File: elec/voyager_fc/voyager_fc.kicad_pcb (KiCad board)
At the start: 6 copper layers, 65 x 56 mm, 173 parts, among them J1 Raspberry Pi 5 Connector, J10 BM04B-GHS-TBT_LF__SN__N_, J11 BM04B-GHS-TBT_LF__SN__N_, J12 BM04B-GHS-TBT_LF__SN__N_, J13 BM04B-GHS-TBT_LF__SN__N_, J14 BM03B-GHS-TBT_LF__SN__N_, J15 BM03B-GHS-TBT_LF__SN__N_, J16 BM03B-GHS-TBT_LF__SN__N_, J17 BM03B-GHS-TBT_LF__SN__N_, J18 BM02B-GHS-TBT_LF__SN__N_, J19 BM02B-GHS-TBT_LF__SN__N_, J2 Pi Power Connect, J20 BM02B-GHS-TBT_LF__SN__N_, J21 BM06B-GHS-TBT_LF__SN__N_, J22 BM06B-GHS-TBT_LF__SN__N_, J23 BM06B-GHS-TBT_LF__SN__N_, J24 AUX Leak, J3 AUX Power Connect, J4 PWM Power Rail 1, J5 PWM GND Rail 1, J6 PWM Signal Rail 1, J7 PWM Power Rail 2, J8 PWM GND Rail 2, J9 PWM Signal Rail 2, Q3 BSS138, Q4 BSS138, Q5 MMBT3906, U1 TCA9548APWR, U10 LTC4311CDC_TRMPBF, U11 LTC4311CDC_TRMPBF, U12 LTC4311CDC_TRMPBF, U13 LTC4311CDC_TRMPBF, U14 TXS0102YZP, U15 TXS0102YZP, U16 TXS0102YZP, U17 TXS0102YZP, U2 PCA9685PW, U3 PCA9685PW, U4 BME680, U5 ICM-20948, U6 TPS2121RUXR, U7 AMS1117-3.3, U8 ADS1015IDGS, U9 AMS1117-1.8, X1 SG-8002CE

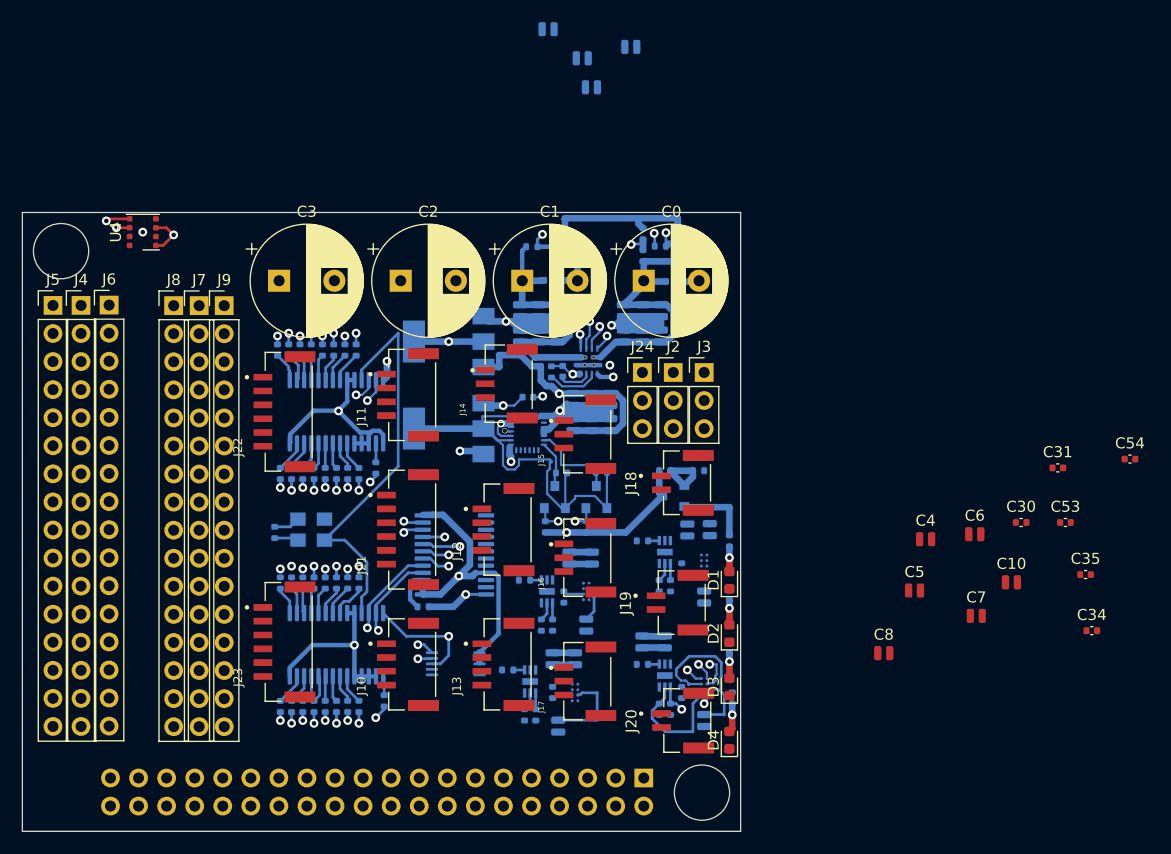
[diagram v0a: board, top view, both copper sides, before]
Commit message: Place all components and start route
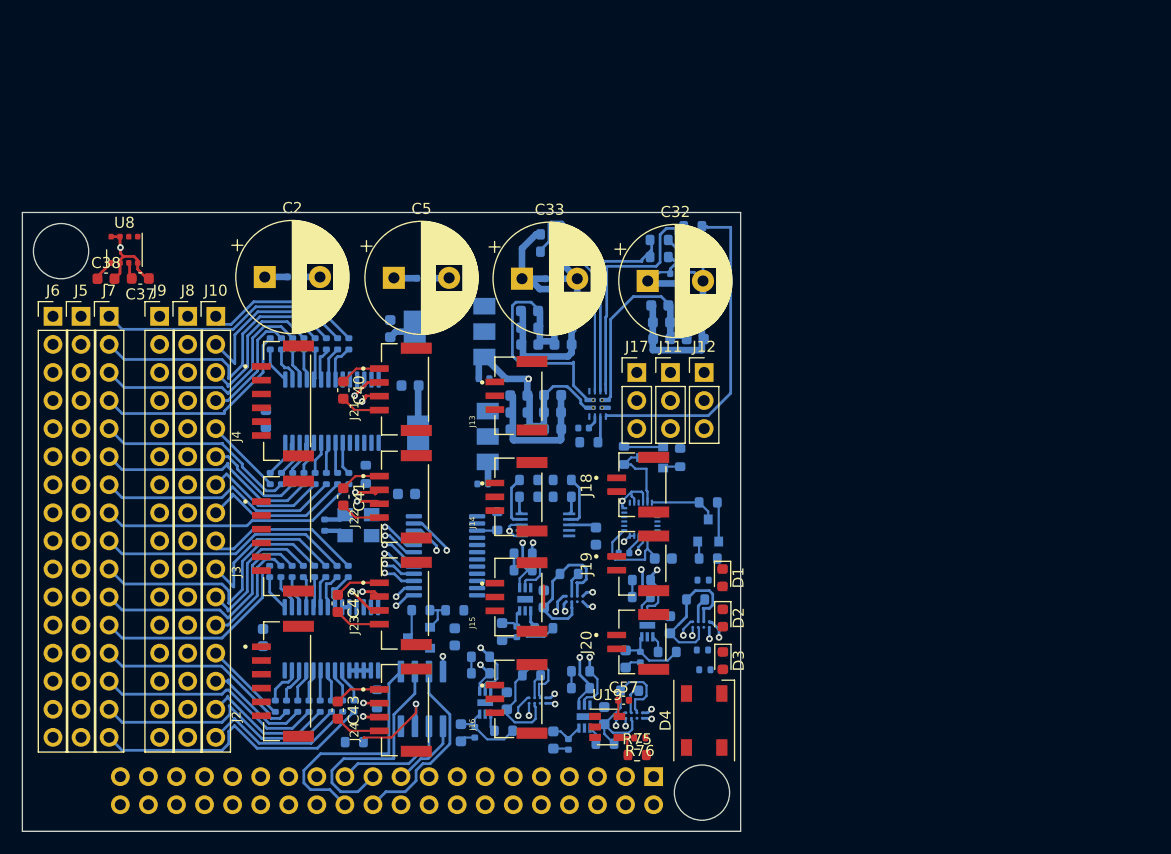
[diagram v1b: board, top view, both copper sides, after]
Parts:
- removed C0: 4700uF, Capacitor_THT:CP_Radial_D10.0mm_P5.00mm
- removed Q4: BSS138, Package_TO_SOT_SMD:SOT-23
- removed Q5: MMBT3906, Package_TO_SOT_SMD:SOT-23
- removed R0: 10k, Resistor_SMD:R_0402_1005Metric
- added C47: 10uF, Capacitor_SMD:C_0603_1608Metric, B.Cu at (161.2, 110.8)
- added C55: 10uF, Capacitor_SMD:C_0603_1608Metric, B.Cu at (176.4, 110.1)
- added C56: 10uF, Capacitor_SMD:C_0603_1608Metric, B.Cu at (170.4, 118.4)
- added C57: 100nF, Capacitor_SMD:C_0402_1005Metric, F.Cu at (172.2, 117.0)
- added Q1: MMBT3906, Package_TO_SOT_SMD:SOT-23, B.Cu at (153.7, 111.3)
- added Q2: BSS138, Package_TO_SOT_SMD:SOT-23, B.Cu at (174.8, 95.0)
- added R1: 220, Resistor_SMD:R_0402_1005Metric, B.Cu at (179.4, 106.1)
- added R4: 220, Resistor_SMD:R_0402_1005Metric, B.Cu at (147.8, 117.5)
- added R5: 220, Resistor_SMD:R_0402_1005Metric, B.Cu at (146.7, 117.5)
- added R6: 220, Resistor_SMD:R_0402_1005Metric, B.Cu at (145.7, 117.5)
- added R7: 220, Resistor_SMD:R_0402_1005Metric, B.Cu at (144.7, 117.5)
- added R75: 470, Resistor_SMD:R_0603_1608Metric, F.Cu at (173.4, 121.9)
- added R76: 470, Resistor_SMD:R_0402_1005Metric, F.Cu at (173.6, 120.4)
- added U18: TXS0102YZP, Package_BGA:Texas_DSBGA-8_0.9x1.9mm_Layout2x4_P0.5mm, B.Cu at (179.2, 110.1)
- added U19: SN74LV1T34DBV, Package_TO_SOT_SMD:SOT-23-5, F.Cu at (170.7, 119.4)
- C1: value 4700uF -> 0.1uF; footprint Capacitor_THT:CP_Radial_D10.0mm_P5.00mm -> Capacitor_SMD:C_0402_1005Metric; moved to B.Cu
- C10, C6, C7, C8: footprint Capacitor_SMD:C_0504_1310Metric -> Capacitor_SMD:C_0603_1608Metric; moved to B.Cu
- C11: value 1nF -> 10uF; footprint Capacitor_SMD:C_0402_1005Metric -> Capacitor_SMD:C_0603_1608Metric
- C12, C13, C14, C15, C16, C17, C18, C21, C23, C24, C25, C26, C27, C28, C29, C44, C45, C46, C48: footprint Capacitor_SMD:C_0504_1310Metric -> Capacitor_SMD:C_0603_1608Metric
- C19, C22: value 10uF -> 1uF; footprint Capacitor_SMD:C_0504_1310Metric -> Capacitor_SMD:C_0402_1005Metric
- C20: value 10uF -> 1nF; footprint Capacitor_SMD:C_0504_1310Metric -> Capacitor_SMD:C_0402_1005Metric
- C3: value 4700uF -> 10uF; footprint Capacitor_THT:CP_Radial_D10.0mm_P5.00mm -> Capacitor_SMD:C_0603_1608Metric; moved to B.Cu
- C30: value 10uF -> 0.1uF; moved to B.Cu
- C31: value 1uF -> 0.1uF; moved to B.Cu
- C32, C33: value 0.1uF -> 4700uF; footprint Capacitor_SMD:C_0402_1005Metric -> Capacitor_THT:CP_Radial_D10.0mm_P5.00mm; moved to F.Cu
- C34, C35: value 0.1uF -> 10uF; footprint Capacitor_SMD:C_0402_1005Metric -> Capacitor_SMD:C_0603_1608Metric; moved to B.Cu
- C36: value 10uF -> 0.1uf; footprint Capacitor_SMD:C_0504_1310Metric -> Capacitor_SMD:C_0402_1005Metric
- C37, C41, C43: value 0.1uF -> 10uF; footprint Capacitor_SMD:C_0504_1310Metric -> Capacitor_SMD:C_0603_1608Metric; moved to F.Cu
- C38, C40, C42: footprint Capacitor_SMD:C_0504_1310Metric -> Capacitor_SMD:C_0603_1608Metric; moved to F.Cu
- C39: value 0.1uF -> 10uF; footprint Capacitor_SMD:C_0504_1310Metric -> Capacitor_SMD:C_0603_1608Metric
- C4: value 10uF -> 0.1uF; footprint Capacitor_SMD:C_0504_1310Metric -> Capacitor_SMD:C_0402_1005Metric; moved to B.Cu
- C49, C50, C51, C52: value 10uF -> 0.1uF; footprint Capacitor_SMD:C_0504_1310Metric -> Capacitor_SMD:C_0402_1005Metric
- C5: value 10uF -> 4700uF; footprint Capacitor_SMD:C_0504_1310Metric -> Capacitor_THT:CP_Radial_D10.0mm_P5.00mm
- C53: value 1uF -> 10uF; footprint Capacitor_SMD:C_0402_1005Metric -> Capacitor_SMD:C_0603_1608Metric; moved to B.Cu
- C54: footprint Capacitor_SMD:C_0402_1005Metric -> Capacitor_SMD:C_0603_1608Metric; moved to B.Cu
- C9: value 0.1uf -> 10uF; footprint Capacitor_SMD:C_0402_1005Metric -> Capacitor_SMD:C_0603_1608Metric
- D1: value WHITE -> RED
- D2: value RED -> YELLOW
- D3: value YELLOW -> WHITE
- D4: value GREEN -> SK6812; footprint LED_SMD:LED_0603_1608Metric -> LED_SMD:LED_SK6812_PLCC4_5.0x5.0mm_P3.2mm
- J10: value BM04B-GHS-TBT_LF__SN__N_ -> PWM Signal Rail 1; footprint BM04B-GHS-TBT_LF__SN__N_:JST_BM04B-GHS-TBT_LF__SN__N_ -> Connector_PinHeader_2.54mm:PinHeader_1x16_P2.54mm_Vertical
- J11: value BM04B-GHS-TBT_LF__SN__N_ -> Pi Power Connect; footprint BM04B-GHS-TBT_LF__SN__N_:JST_BM04B-GHS-TBT_LF__SN__N_ -> Connector_PinHeader_2.54mm:PinHeader_1x03_P2.54mm_Vertical
- J12: value BM04B-GHS-TBT_LF__SN__N_ -> AUX Power Connect; footprint BM04B-GHS-TBT_LF__SN__N_:JST_BM04B-GHS-TBT_LF__SN__N_ -> Connector_PinHeader_2.54mm:PinHeader_1x03_P2.54mm_Vertical
- J13: value BM04B-GHS-TBT_LF__SN__N_ -> BM03B-GHS-TBT_LF__SN__N_; footprint BM04B-GHS-TBT_LF__SN__N_:JST_BM04B-GHS-TBT_LF__SN__N_ -> BM03B-GHS-TBT_LF__SN__N_:CONN_BM03B-GHS-TBT_LF__SN__N_
- J17: value BM03B-GHS-TBT_LF__SN__N_ -> AUX Leak; footprint BM03B-GHS-TBT_LF__SN__N_:CONN_BM03B-GHS-TBT_LF__SN__N_ -> Connector_PinHeader_2.54mm:PinHeader_1x03_P2.54mm_Vertical
- J2: value Pi Power Connect -> BM06B-GHS-TBT_LF__SN__N_; footprint Connector_PinHeader_2.54mm:PinHeader_1x03_P2.54mm_Vertical -> BM06B-GHS-TBT_LF__SN__N_:JST_BM06B-GHS-TBT_LF__SN__N_
- J21, J22, J23: value BM06B-GHS-TBT_LF__SN__N_ -> BM04B-GHS-TBT_LF__SN__N_; footprint BM06B-GHS-TBT_LF__SN__N_:JST_BM06B-GHS-TBT_LF__SN__N_ -> BM04B-GHS-TBT_LF__SN__N_:JST_BM04B-GHS-TBT_LF__SN__N_
- J24: value AUX Leak -> BM04B-GHS-TBT_LF__SN__N_; footprint Connector_PinHeader_2.54mm:PinHeader_1x03_P2.54mm_Vertical -> BM04B-GHS-TBT_LF__SN__N_:JST_BM04B-GHS-TBT_LF__SN__N_
- J3: value AUX Power Connect -> BM06B-GHS-TBT_LF__SN__N_; footprint Connector_PinHeader_2.54mm:PinHeader_1x03_P2.54mm_Vertical -> BM06B-GHS-TBT_LF__SN__N_:JST_BM06B-GHS-TBT_LF__SN__N_
- J4: value PWM Power Rail 1 -> BM06B-GHS-TBT_LF__SN__N_; footprint Connector_PinHeader_2.54mm:PinHeader_1x16_P2.54mm_Vertical -> BM06B-GHS-TBT_LF__SN__N_:JST_BM06B-GHS-TBT_LF__SN__N_
- J5: value PWM GND Rail 1 -> PWM Power Rail 2
- J6: value PWM Signal Rail 1 -> PWM GND Rail 2
- J7: value PWM Power Rail 2 -> PWM Signal Rail 2
- J8: value PWM GND Rail 2 -> PWM Power Rail 1
- J9: value PWM Signal Rail 2 -> PWM GND Rail 1
- R10, R11, R2, R8, R9: value 10k -> 220
- R20: value 220 -> 200
- R21, R55, R56, R57: value 220 -> 10k; footprint Resistor_SMD:R_0402_1005Metric -> Resistor_SMD:R_0603_1608Metric
- R3, R59, R60, R61, R62, R63, R64, R65, R66, R67, R68, R69, R70, R71, R72, R73, R74: footprint Resistor_SMD:R_0402_1005Metric -> Resistor_SMD:R_0603_1608Metric
- R38: value 220 -> 4.99k; footprint Resistor_SMD:R_0402_1005Metric -> Resistor_SMD:R_0603_1608Metric
- R39, R41: value 220 -> 1.15k; footprint Resistor_SMD:R_0402_1005Metric -> Resistor_SMD:R_0603_1608Metric
- R40: value 220 -> 4.99K; footprint Resistor_SMD:R_0402_1005Metric -> Resistor_SMD:R_0603_1608Metric
- R42: value 220 -> 4.32k; footprint Resistor_SMD:R_0402_1005Metric -> Resistor_SMD:R_0603_1608Metric
- R43: value 220 -> 10.2k; footprint Resistor_SMD:R_0402_1005Metric -> Resistor_SMD:R_0603_1608Metric
- R44: value 1K -> 36.5k; footprint Resistor_SMD:R_0402_1005Metric -> Resistor_SMD:R_0603_1608Metric
- R45: value 20K -> 19.6k; footprint Resistor_SMD:R_0402_1005Metric -> Resistor_SMD:R_0603_1608Metric
- R46: value 220 -> 470k; footprint Resistor_SMD:R_0402_1005Metric -> Resistor_SMD:R_0603_1608Metric
- R47: value 4.99K -> 470k; footprint Resistor_SMD:R_0402_1005Metric -> Resistor_SMD:R_0603_1608Metric
- R48: value 4.32k -> 470k; footprint Resistor_SMD:R_0402_1005Metric -> Resistor_SMD:R_0603_1608Metric
- R49: value 36.5k -> 470k; footprint Resistor_SMD:R_0402_1005Metric -> Resistor_SMD:R_0603_1608Metric
- R50: value 1.15k -> 20K; footprint Resistor_SMD:R_0402_1005Metric -> Resistor_SMD:R_0603_1608Metric
- R51: value 10.2k -> 1K; footprint Resistor_SMD:R_0402_1005Metric -> Resistor_SMD:R_0603_1608Metric
- R52: value 4.99k -> 220
- R53: value 1.15k -> 10k; footprint Resistor_SMD:R_0402_1005Metric -> Resistor_SMD:R_0603_1608Metric
- R54: value 19.6k -> 10k; footprint Resistor_SMD:R_0402_1005Metric -> Resistor_SMD:R_0603_1608Metric
- R58: value 200 -> 10k; footprint Resistor_SMD:R_0402_1005Metric -> Resistor_SMD:R_0603_1608Metric
- U1: value TCA9548APWR -> PCA9685PW; footprint Package_SO:TSSOP-24_4.4x7.8mm_P0.65mm -> Package_SO:TSSOP-28_4.4x9.7mm_P0.65mm
- U10: value LTC4311CDC_TRMPBF -> TCA9548APWR; footprint footprint:DFN-6_DC -> Package_SO:TSSOP-24_4.4x7.8mm_P0.65mm
- U14: value TXS0102YZP -> LTC4311CDC_TRMPBF; footprint Package_BGA:Texas_DSBGA-8_0.9x1.9mm_Layout2x4_P0.5mm -> footprint:DFN-6_DC
- U3: value PCA9685PW -> AMS1117-1.8; footprint Package_SO:TSSOP-28_4.4x9.7mm_P0.65mm -> Package_TO_SOT_SMD:SOT-223-3_TabPin2
- U4: value BME680 -> TPS2121RUXR; footprint Package_LGA:Bosch_LGA-8_3x3mm_P0.8mm_ClockwisePinNumbering -> TPS2121RUXR:IC_TPS2121RUXR; moved to B.Cu
- U5: value ICM-20948 -> AMS1117-3.3; footprint Sensor_Motion:InvenSense_QFN-24_3x3mm_P0.4mm -> Package_TO_SOT_SMD:SOT-223-3_TabPin2
- U6: value TPS2121RUXR -> ADS1015IDGS; footprint TPS2121RUXR:IC_TPS2121RUXR -> Package_SO:TSSOP-10_3x3mm_P0.5mm
- U7: value AMS1117-3.3 -> ICM-20948; footprint Package_TO_SOT_SMD:SOT-223-3_TabPin2 -> Sensor_Motion:InvenSense_QFN-24_3x3mm_P0.4mm
- U8: value ADS1015IDGS -> BME680; footprint Package_SO:TSSOP-10_3x3mm_P0.5mm -> Package_LGA:Bosch_LGA-8_3x3mm_P0.8mm_ClockwisePinNumbering; moved to F.Cu
- U9: value AMS1117-1.8 -> MB85RS512T; footprint Package_TO_SOT_SMD:SOT-223-3_TabPin2 -> MB85RS512TPNF-G-JNERE1:SOIC127P600X88-8N
- moved C6 65.1 mm to (139.5, 111.3), turned to 90 degrees
- moved C46 64.2 mm to (157.5, 119.9), turned to 270 degrees
- moved C45 63.1 mm to (165.8, 120.6), turned to 270 degrees
- moved C4 62.0 mm to (142.3, 78.7)
- moved C38 60.3 mm to (125.3, 78.8), turned to 0 degrees
- moved C5 55.0 mm to (151.4, 78.7)
- moved C54 54.5 mm to (165.0, 107.8), turned to 90 degrees
- moved C48 54.5 mm to (172.4, 113.2), turned to 270 degrees
- moved C53 53.1 mm to (161.6, 117.0), turned to 90 degrees
- moved C37 52.3 mm to (128.4, 78.8), turned to 180 degrees
- moved C31 49.0 mm to (165.6, 78.8)
- moved U8 48.0 mm to (127.0, 76.2), turned to 0 degrees
- moved C10 46.7 mm to (166.7, 83.2)
- moved C34 45.7 mm to (169.7, 102.1), turned to 90 degrees
- moved U4 44.0 mm to (169.8, 90.1), turned to 0 degrees
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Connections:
- net PI_CE1 renamed Net-(J1-Pad26)
- net PI_CLK renamed Net-(J1-Pad12)
- net PI_DIN renamed Net-(J1-Pad38)
- net PI_DOUT renamed Net-(J1-Pad40)
- net PI_FS renamed Net-(J1-Pad35)
- net PI_GPIO22 renamed Net-(J1-Pad15)
- net PI_GPIO23 renamed Net-(J1-Pad16)
- net PI_GPIO24 renamed Net-(J1-Pad18)
- net PI_GPIO27 renamed Net-(J1-Pad13)
- net PI_GPIO4 renamed Net-(J1-Pad7)
- net PI_IDSC renamed Net-(J1-Pad28)
- net PI_IDSD renamed Net-(J1-Pad27)
- C1 pad 1: 5VAux -> +5V
- C10 pad 1: GND -> /PREG/5VAux
- C10 pad 2: +5V -> GND
- C11 pad 1: Net-(C11-Pad1) -> /PREG/5VMain
- C12 pad 1: 5VAux -> /PREG/5VAux
- C13 pad 1: 5VAux -> /PREG/5VMain
- C14 pad 1: 5VAux -> /PREG/5VAux
- C15 pad 1: 5VAux -> /PREG/5VMain
- C16 pad 1: 5VAux -> /PREG/5VAux
- C17 pad 1: 5VAux -> /PREG/5VMain
- C18 pad 1: 5VMain -> /PREG/5VAux
- C19 pad 1: 5VMain -> +3V3
- C20 pad 1: 5VMain -> Net-(C20-Pad1)
- C21 pad 1: 5VMain -> GND
- C21 pad 2: GND -> +1V8
- C22 pad 1: 5VMain -> +5V
- C23 pad 1: 5VMain -> +5V
- C25 pad 1: +5V -> GND
- C25 pad 2: GND -> +3V3
- C3 pad 1: +5V -> GND
- C3 pad 2: GND -> +5V
- C30 pad 1: GND -> /PREG/5VMain
- C30 pad 2: +3V3 -> GND
- C31 pad 1: +5V -> /PREG/5VAux
- C32 pad 1: 5VMain -> /PREG/5VMain
- C33 pad 1: 5VAux -> /PREG/5VAux
- C34 pad 1: +5V -> GND
- C34 pad 2: GND -> +5V
- C35 pad 1: +5V -> GND
- C35 pad 2: GND -> +1V8
- C36 pad 1: +3V3 -> GND
- C36 pad 2: GND -> Net-(C36-Pad2)
- C37 pad 1: +3V3 -> GND
- C37 pad 2: GND -> +3V3
- C4 pad 1: +3V3 -> +5V
- C40 pad 1: +3V3 -> +5V
- C41 pad 1: +3V3 -> +5V
- C42 pad 1: +3V3 -> +5V
- C43 pad 1: +3V3 -> +5V
- C44 pad 1: +5V -> +3V3
- C45 pad 1: +5V -> +3V3
- C46 pad 1: +5V -> +3V3
- C48 pad 1: +5V -> +3V3
- C49 pad 1: Net-(C49-Pad1) -> +3V3
- C49 pad 2: +3V3 -> GND
- C5 pad 1: GND -> +5V
- C5 pad 2: +5V -> GND
- C50 pad 1: Net-(C50-Pad1) -> +3V3
- C50 pad 2: +3V3 -> GND
- C51 pad 1: Net-(C51-Pad1) -> +3V3
- C51 pad 2: +3V3 -> GND
- C52 pad 1: Net-(C52-Pad1) -> +3V3
- C52 pad 2: +3V3 -> GND
- C54 pad 1: GND -> +3V3
- C54 pad 2: +1V8 -> GND
- C7 pad 1: GND -> /PREG/5VMain
- C7 pad 2: +3V3 -> GND
- C8 pad 1: +3V3 -> /PREG/5VAux
- C9 pad 1: GND -> /PREG/5VMain
- C9 pad 2: Net-(C9-Pad2) -> GND
- J1 pad 10: PI_RXD -> /PI_RXD0
- J1 pad 11: PI_GPIO17 -> /PI_RXD1
- J1 pad 17: PION -> /SOFTON
- J1 pad 19: PI_MOSI -> /MOSI
- J1 pad 21: PI_MISO -> /MISO
- J1 pad 22: PI_GPIO25 -> /WP
- J1 pad 23: PI_SCLK -> /SCLK
- J1 pad 24: PI_CE0 -> /CE0
- J1 pad 29: PI_GPIO5 -> /NEODIN
- J1 pad 3: PI_SDA -> /PI_SDA
- J1 pad 31: PI_GPIO6 -> /NEORGBDIN
- J1 pad 32: PI_GPIO12 -> /PI_TXD2
- J1 pad 33: PI_GPIO13 -> /PI_RXD2
- J1 pad 36: PI_GPIO16 -> /PI_TXD1
- J1 pad 37: PI_GPIO26 -> /LEAKIN
- J1 pad 5: PI_SCL -> /PI_SCL
- J1 pad 8: PI_TXD -> /PI_TXD0
- J10 pad 1: +5V -> /PWM/PWM31
- J10 pad 2: OSC4 -> /PWM/PWM30
- J10 pad 3: OSD4 -> /PWM/PWM29
- J10 pad 4: GND -> /PWM/PWM28
- J11 pad 1: +5V -> /PREG/5VMain
- J11 pad 2: OSC7 -> GND
- J11 pad 3: OSD7 -> GND
- J12 pad 1: +5V -> /PREG/5VAux
- J12 pad 2: OSC6 -> GND
- J12 pad 3: OSD6 -> GND
- J13 pad 1: +5V -> GND
- J13 pad 2: OSC5 -> /ADS/AIN0
- J13 pad 3: OSD5 -> +3V3
- J14 pad 2: AIN0 -> /ADS/AIN1
- J15 pad 2: AIN1 -> /ADS/AIN2
- J16 pad 2: AIN2 -> /ADS/AIN3
- J17 pad 2: AIN3 -> +3V3
- J17 pad 3: +3V3 -> /LEAK/LEAK_
- J18 pad 2: LEAK_IN -> /LEAK/LEAK_
- J19 pad 2: LEAK_IN -> /LEAK/LEAK_
- J2 pad 1: 5VMain -> +5V
- J2 pad 2: GND -> /PI_TXD0
- J2 pad 3: GND -> /PI_RXD0
- J20 pad 2: LEAK_IN -> /LEAK/LEAK_
- J21 pad 2: PI_TXD -> /I2C/OSC4
- J21 pad 3: PI_RXD -> /I2C/OSD4
- J21 pad 4: Net-(J21-Pad4) -> GND
- J22 pad 2: PI_GPIO16 -> /I2C/OSC5
- J22 pad 3: PI_GPIO17 -> /I2C/OSD5
- J22 pad 4: Net-(J22-Pad4) -> GND
- J23 pad 2: PI_GPIO12 -> /I2C/OSC6
- J23 pad 3: PI_GPIO13 -> /I2C/OSD6
- J23 pad 4: Net-(J23-Pad4) -> GND
- J24 pad 1: GND -> +5V
- J24 pad 2: +3V3 -> /I2C/OSC7
- J24 pad 3: LEAK_IN -> /I2C/OSD7
- J3 pad 1: 5VAux -> +5V
- J3 pad 2: GND -> /PI_TXD1
- J3 pad 3: GND -> /PI_RXD1
- J4 pad 2: +5V -> /PI_TXD2
- J4 pad 3: +5V -> /PI_RXD2
- J4 pad 4: +5V -> Net-(J4-Pad4)
- J4 pad 5: +5V -> Net-(J4-Pad5)
- J4 pad 6: +5V -> GND
- J5 pad 1: GND -> +5V
- J5 pad 10: GND -> +5V
- J5 pad 11: GND -> +5V
- J5 pad 12: GND -> +5V
- J5 pad 13: GND -> +5V
- J5 pad 14: GND -> +5V
- J5 pad 15: GND -> +5V
- J5 pad 16: GND -> +5V
- J5 pad 2: GND -> +5V
- J5 pad 3: GND -> +5V
- J5 pad 4: GND -> +5V
- J5 pad 5: GND -> +5V
- J5 pad 6: GND -> +5V
- J5 pad 7: GND -> +5V
- J5 pad 8: GND -> +5V
- J5 pad 9: GND -> +5V
- J6 pad 1: PWM15 -> GND
- J6 pad 10: PWM6 -> GND
- J6 pad 11: PWM5 -> GND
- J6 pad 12: PWM4 -> GND
- J6 pad 13: PWM3 -> GND
- J6 pad 14: PWM2 -> GND
- J6 pad 15: PWM1 -> GND
- J6 pad 16: PWM0 -> GND
- J6 pad 2: PWM14 -> GND
- J6 pad 3: PWM13 -> GND
- J6 pad 4: PWM12 -> GND
- J6 pad 5: PWM11 -> GND
- J6 pad 6: PWM10 -> GND
- J6 pad 7: PWM9 -> GND
- J6 pad 8: PWM8 -> GND
- J6 pad 9: PWM7 -> GND
- J7 pad 1: +5V -> /PWM/PWM15
- J7 pad 10: +5V -> /PWM/PWM6
- J7 pad 11: +5V -> /PWM/PWM5
- J7 pad 12: +5V -> /PWM/PWM4
- J7 pad 13: +5V -> /PWM/PWM3
- J7 pad 14: +5V -> /PWM/PWM2
- J7 pad 15: +5V -> /PWM/PWM1
- J7 pad 16: +5V -> /PWM/PWM0
- J7 pad 2: +5V -> /PWM/PWM14
- J7 pad 3: +5V -> /PWM/PWM13
- J7 pad 4: +5V -> /PWM/PWM12
- J7 pad 5: +5V -> /PWM/PWM11
- J7 pad 6: +5V -> /PWM/PWM10
- J7 pad 7: +5V -> /PWM/PWM9
- J7 pad 8: +5V -> /PWM/PWM8
- J7 pad 9: +5V -> /PWM/PWM7
- J8 pad 1: GND -> +5V
- J8 pad 10: GND -> +5V
- J8 pad 11: GND -> +5V
- J8 pad 12: GND -> +5V
- J8 pad 13: GND -> +5V
- J8 pad 14: GND -> +5V
- J8 pad 15: GND -> +5V
- J8 pad 16: GND -> +5V
- J8 pad 2: GND -> +5V
- J8 pad 3: GND -> +5V
- J8 pad 4: GND -> +5V
- J8 pad 5: GND -> +5V
- J8 pad 6: GND -> +5V
- J8 pad 7: GND -> +5V
- J8 pad 8: GND -> +5V
- J8 pad 9: GND -> +5V
- J9 pad 1: PWM31 -> GND
- J9 pad 10: PWM22 -> GND
- J9 pad 11: PWM21 -> GND
- J9 pad 12: PWM20 -> GND
- J9 pad 13: PWM19 -> GND
- J9 pad 14: PWM18 -> GND
- J9 pad 15: PWM17 -> GND
- J9 pad 16: PWM16 -> GND
- J9 pad 2: PWM30 -> GND
- J9 pad 3: PWM29 -> GND
- J9 pad 4: PWM28 -> GND
- J9 pad 5: PWM27 -> GND
- J9 pad 6: PWM26 -> GND
- J9 pad 7: PWM25 -> GND
- J9 pad 8: PWM24 -> GND
- J9 pad 9: PWM23 -> GND
- Q3 pad 2: SD2 -> /SDIMU
- Q3 pad 3: SDL21v8 -> /IMU/SDL21V8
- R10 pad 1: +1V8 -> Net-(R10-Pad1)
- R10 pad 2: SCL21v8 -> /PWM/PWM3
- R11 pad 1: +1V8 -> Net-(R11-Pad1)
- R11 pad 2: SDL21v8 -> /PWM/PWM19
- R12 pad 2: PWM0 -> /PWM/PWM4
- R13 pad 2: PWM16 -> /PWM/PWM20
- R14 pad 2: PWM1 -> /PWM/PWM5
- R15 pad 2: PWM17 -> /PWM/PWM21
- R16 pad 2: PWM2 -> /PWM/PWM6
- R17 pad 2: PWM18 -> /PWM/PWM22
- R18 pad 2: PWM3 -> /PWM/PWM7
- R19 pad 2: PWM19 -> /PWM/PWM23
- R2 pad 1: +3V3 -> Net-(D2-Pad2)
- R2 pad 2: Net-(R2-Pad2) -> /SOFTON
- R20 pad 2: PWM4 -> +5V
- R21 pad 1: Net-(R21-Pad1) -> +3V3
- R21 pad 2: PWM20 -> Net-(R21-Pad2)
- R22 pad 2: PWM5 -> /PWM/PWM8
- R23 pad 2: PWM21 -> /PWM/PWM24
- R24 pad 2: PWM6 -> /PWM/PWM9
- R25 pad 2: PWM22 -> /PWM/PWM25
- R26 pad 2: PWM7 -> /PWM/PWM10
- R27 pad 2: PWM23 -> /PWM/PWM26
- R28 pad 2: PWM8 -> /PWM/PWM11
- R29 pad 2: PWM24 -> /PWM/PWM27
- R30 pad 2: PWM9 -> /PWM/PWM12
- R31 pad 2: PWM25 -> /PWM/PWM28
- R32 pad 2: PWM10 -> /PWM/PWM13
- R33 pad 2: PWM26 -> /PWM/PWM29
- R34 pad 2: PWM11 -> /PWM/PWM14
- R35 pad 2: PWM27 -> /PWM/PWM30
- R36 pad 2: PWM12 -> /PWM/PWM15
- R37 pad 2: PWM28 -> /PWM/PWM31
- R38 pad 1: Net-(R38-Pad1) -> /PREG/5VAux
- R38 pad 2: PWM13 -> /PREG/PMUX_OV2
- R39 pad 1: Net-(R39-Pad1) -> /PREG/PMUX_OV2
- R39 pad 2: PWM29 -> GND
- R40 pad 1: Net-(R40-Pad1) -> /PREG/5VMain
- R40 pad 2: PWM14 -> /PREG/PMUX_OV1
- R41 pad 1: Net-(R41-Pad1) -> /PREG/PMUX_OV1
- R41 pad 2: PWM30 -> GND
- R42 pad 1: Net-(R42-Pad1) -> /PREG/5VMain
- R42 pad 2: PWM15 -> /PREG/PMUX_PR1
- R43 pad 1: Net-(R43-Pad1) -> /PREG/PMUX_PR1
- R43 pad 2: PWM31 -> GND
- R44 pad 1: Net-(Q5-Pad1) -> /PREG/PMUX_ST
- R44 pad 2: LEAK_IN -> /PREG/PMUX_PR1
- R45 pad 1: +3V3 -> Net-(R45-Pad1)
- R45 pad 2: Net-(Q5-Pad1) -> GND
- R46 pad 1: PI_GPIO5 -> /ADS/AIN0
- R46 pad 2: Net-(D1-Pad2) -> GND
- R47 pad 1: 5VMain -> /ADS/AIN1
- R47 pad 2: PMUX_OV1 -> GND
- R48 pad 1: 5VMain -> /ADS/AIN2
- R48 pad 2: PMUX_PR1 -> GND
- R49 pad 1: PMUX_ST -> /ADS/AIN3
- R49 pad 2: PMUX_PR1 -> GND
- R50 pad 1: PMUX_OV1 -> +3V3
- R50 pad 2: GND -> Net-(Q1-Pad1)
- R51 pad 1: PMUX_PR1 -> Net-(Q1-Pad1)
- R51 pad 2: GND -> /LEAK/LEAK_
- R52 pad 1: 5VAux -> /LEAKIN
- R52 pad 2: PMUX_OV2 -> Net-(D3-Pad2)
- R53 pad 1: PMUX_OV2 -> +3V3
- R53 pad 2: GND -> /SCIMU
- R54 pad 1: Net-(R54-Pad1) -> +3V3
- R54 pad 2: GND -> /SDIMU
- R55 pad 1: Net-(D2-Pad2) -> +1V8
- R55 pad 2: +5V -> /IMU/SCL21V8
- R56 pad 1: Net-(D3-Pad2) -> +1V8
- R56 pad 2: PION -> /IMU/SDL21V8
- R57 pad 1: Net-(D4-Pad2) -> Net-(R57-Pad1)
- R57 pad 2: PI_GPIO14 -> +3V3
- R58 pad 2: +5V -> +3V3
- R60 pad 1: SC4 -> Net-(R60-Pad1)
- R61 pad 1: +3V3 -> Net-(R61-Pad1)
- R61 pad 2: SD4 -> +3V3
- R63 pad 2: SD5 -> /I2C/SC4
- R64 pad 1: SC5 -> /I2C/SD4
- R65 pad 1: Net-(R65-Pad1) -> +3V3
- R65 pad 2: +3V3 -> /I2C/SC5
- R66 pad 1: SC6 -> /I2C/SD5
- R67 pad 2: SD6 -> /I2C/SC6
- R68 pad 1: Net-(R68-Pad1) -> /I2C/SD6
- R69 pad 2: SD7 -> /I2C/SC7
- R70 pad 1: SC7 -> /I2C/SD7
- R8 pad 1: +3V3 -> Net-(R8-Pad1)
- R8 pad 2: SC2 -> /PWM/PWM2
- R9 pad 1: +3V3 -> Net-(R9-Pad1)
- R9 pad 2: SD2 -> /PWM/PWM18
- U1 pad 1: GND -> Net-(R3-Pad2)
- U1 pad 10: SD3 -> Net-(R8-Pad1)
- U1 pad 11: SC3 -> Net-(R9-Pad1)
- U1 pad 12: GND -> Net-(R10-Pad1)
- U1 pad 13: SD4 -> Net-(R11-Pad1)
- U1 pad 14: SC4 -> GND
- U1 pad 15: SD5 -> Net-(R12-Pad1)
- U1 pad 16: SC5 -> Net-(R13-Pad1)
- U1 pad 17: SD6 -> Net-(R14-Pad1)
- U1 pad 18: SC6 -> Net-(R15-Pad1)
- U1 pad 19: SD7 -> Net-(R16-Pad1)
- U1 pad 20: SC7 -> Net-(R17-Pad1)
- U1 pad 21: GND -> Net-(R18-Pad1)
- U1 pad 22: PI_SCL -> Net-(R19-Pad1)
- U1 pad 23: PI_SDA -> GND
- U1 pad 24: +3V3 -> GND
- U1 pad 3: Net-(R0-Pad1) -> GND
- U1 pad 4: SD0 -> GND
- U1 pad 5: SC0 -> GND
- U1 pad 6: SD1 -> Net-(R4-Pad1)
- U1 pad 7: SC1 -> Net-(R5-Pad1)
- U1 pad 8: SD2 -> Net-(R6-Pad1)
- U1 pad 9: SC2 -> Net-(R7-Pad1)
- U10 pad 1: Net-(R59-Pad1) -> GND
- U10 pad 2: Net-(U10-Pad2) -> GND
- U10 pad 3: +3V3 -> Net-(R58-Pad1)
- U10 pad 4: SC4 -> /SDPWM
- U10 pad 5: SD4 -> /SCPWM
- U10 pad 6: GND -> /SDBME
- U10 pad 7: GND -> /SCBME
- U11 pad 1: Net-(R62-Pad1) -> Net-(R59-Pad1)
- U11 pad 4: SC5 -> /I2C/SD4
- U11 pad 5: SD5 -> /I2C/SC4
- U12 pad 1: Net-(R65-Pad1) -> Net-(R60-Pad1)
- U12 pad 4: SC6 -> /I2C/SD5
- U12 pad 5: SD6 -> /I2C/SC5
- U13 pad 1: Net-(R68-Pad1) -> Net-(R61-Pad1)
- U13 pad 4: SC7 -> /I2C/SD6
- U13 pad 5: SD7 -> /I2C/SC6
- U15 pad A1: OSC5 -> /I2C/OSC4
- U15 pad A2: OSD5 -> /I2C/OSD4
- U15 pad B2: Net-(C50-Pad1) -> +3V3
- U15 pad C1: Net-(C50-Pad1) -> +3V3
- U15 pad C2: Net-(R72-Pad1) -> Net-(R71-Pad1)
- U15 pad D1: SC5 -> /I2C/SC4
- U15 pad D2: SD5 -> /I2C/SD4
- U16 pad A1: OSC6 -> /I2C/OSC5
- U16 pad A2: OSD6 -> /I2C/OSD5
- U16 pad B2: Net-(C51-Pad1) -> +3V3
- U16 pad C1: Net-(C51-Pad1) -> +3V3
- U16 pad C2: Net-(R73-Pad1) -> Net-(R72-Pad1)
- U16 pad D1: SC6 -> /I2C/SC5
- U16 pad D2: SD6 -> /I2C/SD5
- U17 pad A1: OSC7 -> /I2C/OSC6
- U17 pad A2: OSD7 -> /I2C/OSD6
- U17 pad B2: Net-(C52-Pad1) -> +3V3
- U17 pad C1: Net-(C52-Pad1) -> +3V3
- U17 pad C2: Net-(R74-Pad1) -> Net-(R73-Pad1)
- U17 pad D1: SC7 -> /I2C/SC6
- U17 pad D2: SD7 -> /I2C/SD6
- U2 pad 1: Net-(R2-Pad2) -> GND
- U2 pad 10: Net-(R16-Pad1) -> Net-(R26-Pad1)
- U2 pad 11: Net-(R17-Pad1) -> Net-(R27-Pad1)
- U2 pad 12: Net-(R18-Pad1) -> Net-(R28-Pad1)
- U2 pad 13: Net-(R19-Pad1) -> Net-(R29-Pad1)
- U2 pad 15: Net-(R20-Pad1) -> Net-(R30-Pad1)
- U2 pad 16: Net-(R21-Pad1) -> Net-(R31-Pad1)
- U2 pad 17: Net-(R22-Pad1) -> Net-(R32-Pad1)
- U2 pad 18: Net-(R23-Pad1) -> Net-(R33-Pad1)
- U2 pad 19: Net-(R24-Pad1) -> Net-(R34-Pad1)
- U2 pad 2: GND -> Net-(R21-Pad2)
- U2 pad 20: Net-(R25-Pad1) -> Net-(R35-Pad1)
- U2 pad 21: Net-(R26-Pad1) -> Net-(R36-Pad1)
- U2 pad 22: Net-(R27-Pad1) -> Net-(R37-Pad1)
- U2 pad 25: PWMCLK -> /PWM/PWMCLK
- U2 pad 26: SC0 -> /SCPWM
- U2 pad 27: SD0 -> /SDPWM
- U2 pad 6: Net-(R12-Pad1) -> Net-(R22-Pad1)
- U2 pad 7: Net-(R13-Pad1) -> Net-(R23-Pad1)
- U2 pad 8: Net-(R14-Pad1) -> Net-(R24-Pad1)
- U2 pad 9: Net-(R15-Pad1) -> Net-(R25-Pad1)
- U3 pad 2: Net-(R3-Pad2) -> +1V8
- U3 pad 3: GND -> +3V3
- U4 pad 1: GND -> +5V
- U4 pad 2: GND -> /PREG/5VAux
- U4 pad 3: SD1 -> +3V3
- U4 pad 4: SC1 -> /PREG/PMUX_OV2
- U4 pad 5: GND -> /PREG/PMUX_OV1
- U4 pad 6: +3V3 -> /PREG/PMUX_PR1
- U4 pad 7: GND -> /PREG/5VMain
- U4 pad 8: +3V3 -> +5V
- U5 pad 1: Net-(U5-Pad1) -> GND
- U5 pad 2: Net-(U5-Pad2) -> +3V3
- U5 pad 3: Net-(U5-Pad3) -> +5V
- U6 pad 1: +5V -> GND
- U6 pad 10: Net-(R54-Pad1) -> /SCADS
- U6 pad 2: 5VAux -> Net-(U6-Pad2)
- U6 pad 3: +3V3 -> GND
- U6 pad 4: PMUX_OV2 -> /ADS/AIN0
- U6 pad 5: PMUX_OV1 -> /ADS/AIN1
- U6 pad 6: PMUX_PR1 -> /ADS/AIN2
- U6 pad 7: 5VMain -> /ADS/AIN3
- U6 pad 9: PMUX_ST -> /SDADS
- U7 pad 1: GND -> Net-(U7-Pad1)
- U7 pad 2: +3V3 -> Net-(U7-Pad2)
- U7 pad 3: +5V -> Net-(U7-Pad3)
- U8 pad 3: GND -> /SDBME
- U8 pad 4: AIN0 -> /SCBME
- U8 pad 5: AIN1 -> GND
- U8 pad 6: AIN2 -> +3V3
- U8 pad 7: AIN3 -> GND
- U8 pad 8: +5V -> +3V3
- U9 pad 1: GND -> /CE0
- U9 pad 2: +1V8 -> /MISO
- U9 pad 3: +3V3 -> /WP
- X1 pad 1: Net-(R58-Pad1) -> Net-(R20-Pad1)
- X1 pad 2: GND1 -> GND
- X1 pad 3: PWMCLK -> /PWM/PWMCLK
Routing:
- net GND: track 534.2 -> 283.2 mm, vias 12 -> 6
- net +5V: track 255.5 -> 161.5 mm, vias 4 -> 1
- net /I2C/OSD4: track 0.00 -> 76.9 mm, vias 0 -> 2
- net /I2C/OSC4: track 0.00 -> 72.1 mm, vias 0 -> 2
- net /PREG/5VAux: track 0.00 -> 65.5 mm
- net SC1: track 62.8 -> 0.00 mm, vias 2 -> 0
- net SD1: track 61.3 -> 0.00 mm, vias 2 -> 0
- net /I2C/OSC5: track 0.00 -> 56.7 mm, vias 0 -> 2
- net 5VAux: track 55.9 -> 0.00 mm
- net /I2C/OSD5: track 0.00 -> 55.0 mm, vias 0 -> 2
- net /I2C/SD7: track 0.00 -> 46.8 mm, vias 0 -> 3
- net /I2C/SC7: track 0.00 -> 46.1 mm, vias 0 -> 3
- net /I2C/SC4: track 0.00 -> 43.1 mm, vias 0 -> 3
- net /PREG/5VMain: track 0.00 -> 42.8 mm
- net /I2C/SD4: track 0.00 -> 42.3 mm, vias 0 -> 3
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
